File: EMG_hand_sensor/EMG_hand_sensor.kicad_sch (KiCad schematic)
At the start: 39 parts, among them J1 Conn_2Rows-07Pins_Shielded, J2 B2B-XH-A, U1 TVS0500DRV, U10 TRS_AUDIO_JACK_3.5mm, U11 TRS_AUDIO_JACK_3.5mm, U2 ADA4099-2xR, U3 CD74HC4067M, U4 TRS_AUDIO_JACK_3.5mm, U6 ADA4099-2xR, U7 LT1762, U8 TRS_AUDIO_JACK_3.5mm

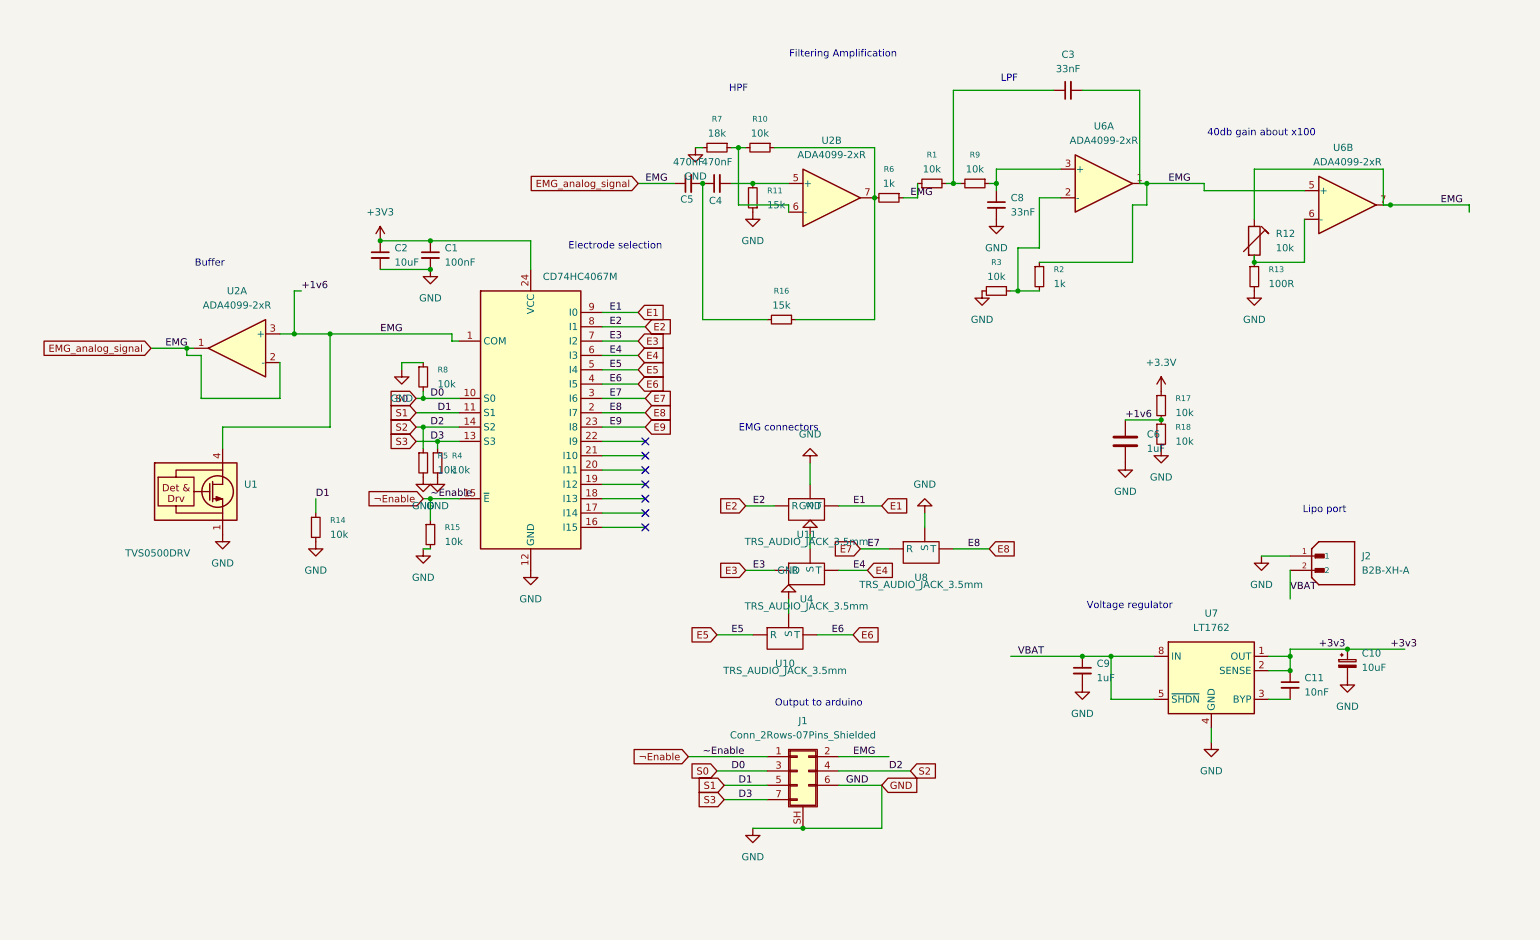
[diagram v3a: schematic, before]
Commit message: completley chnaged from analog to digital
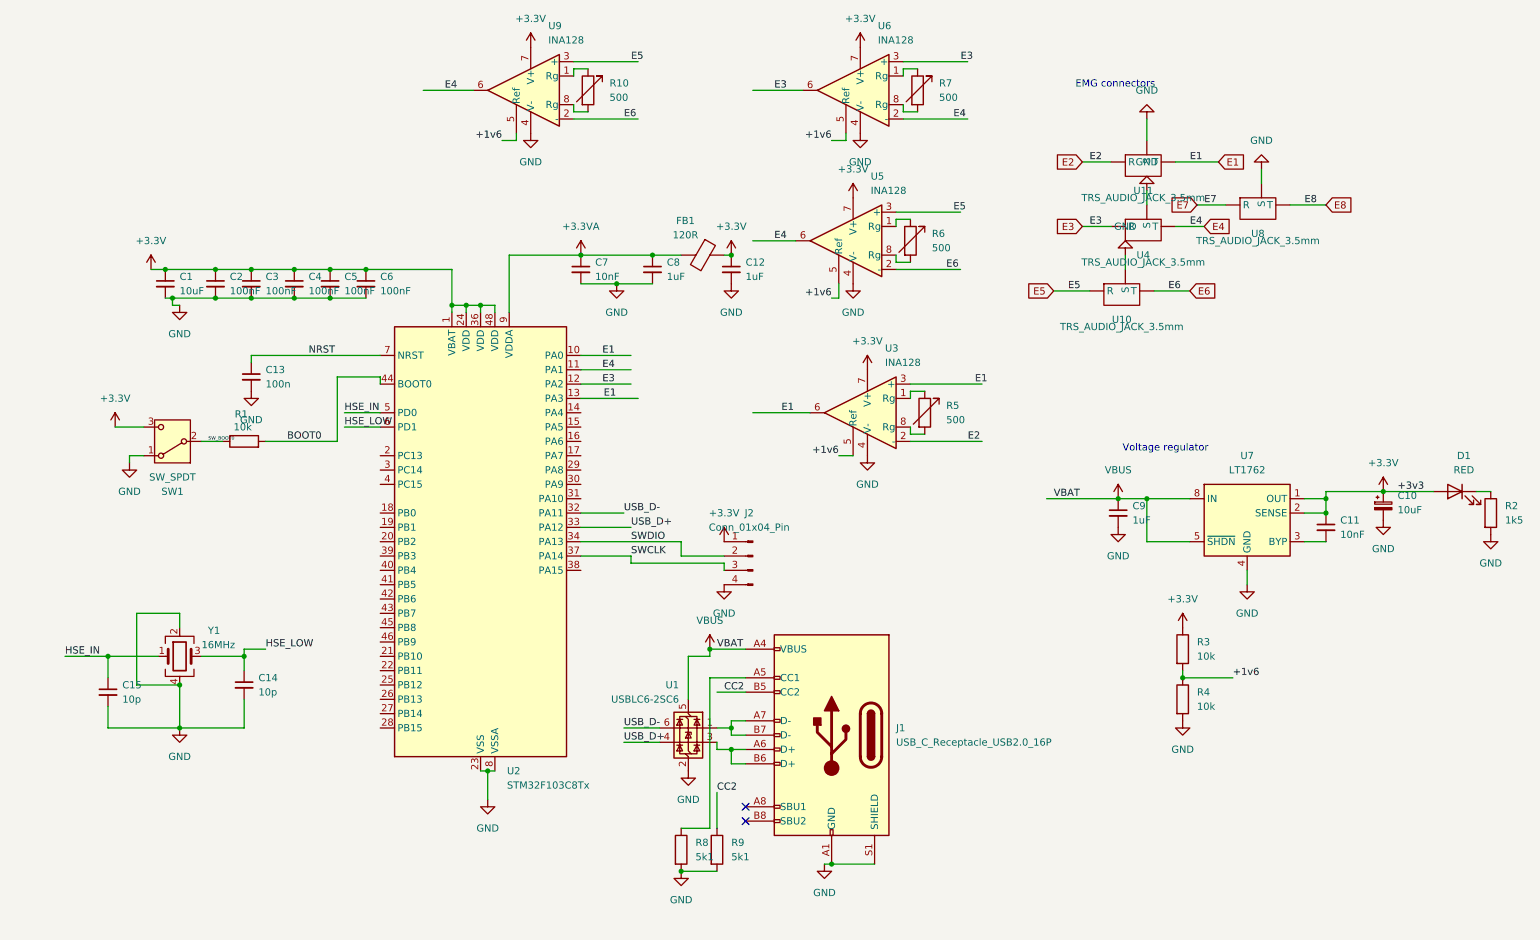
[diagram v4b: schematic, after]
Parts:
- removed C6: 1uF, Capacitor_SMD:C_0805_2012Metric_Pad1.18x1.45mm_HandSolder, symbol Device:C
- removed J1: Conn_2Rows-07Pins_Shielded, Connector_PinHeader_2.54mm:PinHeader_1x07_P2.54mm_Vertical_SMD_Pin1Left, symbol Connector_Generic_Shielded:Conn_2Rows-07Pins_Shielded
- removed J2: B2B-XH-A, Connector_JST:JST_EH_B2B-EH-A_1x02_P2.50mm_Vertical, symbol JST_CONN:B2B-XH-A
- removed R1, R10, R14, R15, R17, R18, R3, R4, R5, R8, R9: 10k, Resistor_SMD:R_0805_2012Metric_Pad1.20x1.40mm_HandSolder, symbol Device:R_Small
- removed R11, R16: 15k, Resistor_SMD:R_0805_2012Metric_Pad1.20x1.40mm_HandSolder, symbol Device:R_Small
- removed R12: 10k, Resistor_SMD:R_0805_2012Metric_Pad1.20x1.40mm_HandSolder, symbol Device:R_Trim
- removed R13: 100R, Resistor_SMD:R_0805_2012Metric_Pad1.20x1.40mm_HandSolder, symbol Device:R_Small
- removed R2, R6: 1k, Resistor_SMD:R_0805_2012Metric_Pad1.20x1.40mm_HandSolder, symbol Device:R_Small
- removed R7: 18k, Resistor_SMD:R_0805_2012Metric_Pad1.20x1.40mm_HandSolder, symbol Device:R_Small
- removed U1: TVS0500DRV, Package_SON:WSON-6-1EP_2x2mm_P0.65mm_EP1x1.6mm, symbol Power_Protection:TVS0500DRV
- removed U2, U6: ADA4099-2xR, Package_SO:SOIC-8_3.9x4.9mm_P1.27mm, symbol Amplifier_Operational:ADA4099-2xR
- removed U3: CD74HC4067M, Package_SO:SOIC-24W_7.5x15.4mm_P1.27mm, symbol 74xx:CD74HC4067M
- added C12: 1uF, symbol Device:C_Small
- added C13: 100n, symbol Device:C_Small
- added C14, C15: 10p, symbol Device:C_Small
- added C6: 100nF, symbol Device:C_Small
- added C7: 10nF, symbol Device:C_Small
- added D1: RED, symbol Device:LED
- added FB1: 120R, symbol Device:FerriteBead
- added J1: USB_C_Receptacle_USB2.0_16P, symbol Connector:USB_C_Receptacle_USB2.0_16P
- added J2: Conn_01x04_Pin, symbol Connector:Conn_01x04_Pin
- added R1, R3, R4: 10k, symbol Device:R
- added R10, R5, R6, R7: 500, symbol Device:R_Variable
- added R2: 1k5, symbol Device:R
- added R8, R9: 5k1, symbol Device:R
- added SW1: SW_SPDT, symbol Switch:SW_SPDT
- added U1: USBLC6-2SC6, Package_TO_SOT_SMD:SOT-23-6, symbol Power_Protection:USBLC6-2SC6
- added U2: STM32F103C8Tx, Package_QFP:LQFP-48_7x7mm_P0.5mm, symbol MCU_ST_STM32F1:STM32F103C8Tx
- added U3, U5, U6, U9: INA128, symbol Amplifier_Instrumentation:INA128
- added Y1: 16MHz, symbol Device:Crystal_GND24
- C1: value 100nF -> 10uF; footprint Capacitor_SMD:C_0805_2012Metric_Pad1.18x1.45mm_HandSolder -> (none)
- C2: value 10uF -> 100nF; footprint Capacitor_SMD:C_0805_2012Metric_Pad1.18x1.45mm_HandSolder -> (none)
- C3: value 33nF -> 100nF; footprint Capacitor_SMD:C_0805_2012Metric_Pad1.18x1.45mm_HandSolder -> (none)
- C4, C5: value 470nF -> 100nF; footprint Capacitor_SMD:C_0805_2012Metric_Pad1.18x1.45mm_HandSolder -> (none)
- C8: value 33nF -> 1uF; footprint Capacitor_SMD:C_0805_2012Metric_Pad1.18x1.45mm_HandSolder -> (none)
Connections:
- net +3V3 is gone; now on net +3.3V: C1.1, C2.1
- net +3v3 is gone; now on net +3.3V: C10.1, C11.1, U7.1 (OUT), U7.2 (SENSE)
- net +3.3V: now also C3.1, C4.1, C5.1, C12.1, C6.1, D1.2 (A), FB1.1, J2.1 (Pin_1), R3.1, SW1.3 (C), U2.1 (VBAT), U2.24 (VDD), U2.36 (VDD), U2.48 (VDD), U3.7 (V+), U5.7 (V+), U6.7 (V+), U9.7 (V+)
- net E1: now also U2.10 (PA0), U2.13 (PA3), U3.3 (+), U3.6
- net E2: now also U3.2 (-)
- net E3: now also U2.12 (PA2), U6.3 (+), U6.6
- net E4: now also U2.11 (PA1), U5.6, U6.2 (-), U9.6
- net E5: now also U5.3 (+), U9.3 (+)
- net E6: now also U5.2 (-), U9.2 (-)
- net GND: now also C3.2, C4.2, C5.2, C12.2, C13.2, C14.2, C15.2, C6.2, C7.2, J1.A1 (GND), J1.A12 (GND), J1.B1 (GND), J1.B12 (GND), J1.S1 (SHIELD), J2.4 (Pin_4), R2.2, R4.2, R8.2, R9.2, SW1.1 (A), U1.2 (GND), U2.23 (VSS), U2.35 (VSS), U2.47 (VSS), U2.8 (VSSA), U3.4 (V-), U5.4 (V-), U6.4 (V-), U9.4 (V-), Y1.2, Y1.4
- net +3.3VA: now reaches C8.1
- net +3.3VA: now also C7.1, FB1.2, U2.9 (VDDA)
- removed net EMG_analog_signal: C3.2, C5.1
- net VBAT renamed VBUS
- net VBUS: now also J1.A4 (VBUS), J1.A9 (VBUS), J1.B4 (VBUS), J1.B9 (VBUS), U1.5 (VBUS)
- new net: R7.1, U6.1 (Rg)
- new net: R7.2, U6.8 (Rg)
- new net: R10.1, U9.1 (Rg)
- new net: R10.2, U9.8 (Rg)
- new net: J1.A5 (CC1), R8.1
- new net: J1.A7 (D-), J1.B7 (D-), U1.1 (I/O1)
- new net: J1.A6 (D+), J1.B6 (D+), U1.3 (I/O2)
- new net: D1.1 (K), R2.1
- new net: R6.1, U5.1 (Rg)
- new net: R6.2, U5.8 (Rg)
- new net: R5.1, U3.1 (Rg)
- new net: R5.2, U3.8 (Rg)
- new net +1v6: R3.2, R4.1, U3.5 (Ref), U5.5 (Ref), U6.5 (Ref), U9.5 (Ref)
- new net BOOT0: R1.2, U2.44 (BOOT0)
- new net CC2: J1.B5 (CC2), R9.1
- new net HSE_IN: C15.1, U2.5 (PD0), Y1.1
- new net HSE_LOW: C14.1, U2.6 (PD1), Y1.3
- new net NRST: C13.1, U2.7 (NRST)
- new net SWCLK: J2.3 (Pin_3), U2.37 (PA14)
- new net SWDIO: J2.2 (Pin_2), U2.34 (PA13)
- new net SW_BOOT0: R1.1, SW1.2 (B)
- new net USB_D+: U1.4 (I/O2), U2.33 (PA12)
- new net USB_D-: U1.6 (I/O1), U2.32 (PA11)
- no-connect marks 7 -> 2
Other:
- note removed: "40db gain about x100"
- note removed: "Buffer"
- note removed: "Electrode selection"
- note removed: "Filtering Amplification"
- note removed: "HPF"
- note removed: "LPF"
- note removed: "Lipo port"
- note removed: "Output to arduino"
- moved on the sheet: C10, C11, C9, U10, U11, U4, U7, U8
